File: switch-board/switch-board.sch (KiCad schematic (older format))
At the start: 52 parts, among them IC1 OPTO-TRANSISTOR4, IC2 OPTO-TRANSISTOR4, IC3 OPTO-TRANSISTOR4, IC4 OPTO-TRANSISTOR4, IC5 OPTO-TRANSISTOR4, IC6 OPTO-TRANSISTOR4, IC7 OPTO-TRANSISTOR4, IC8 OPTO-TRANSISTOR4, P1 CONN_01X04, P2 CONN_01X04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

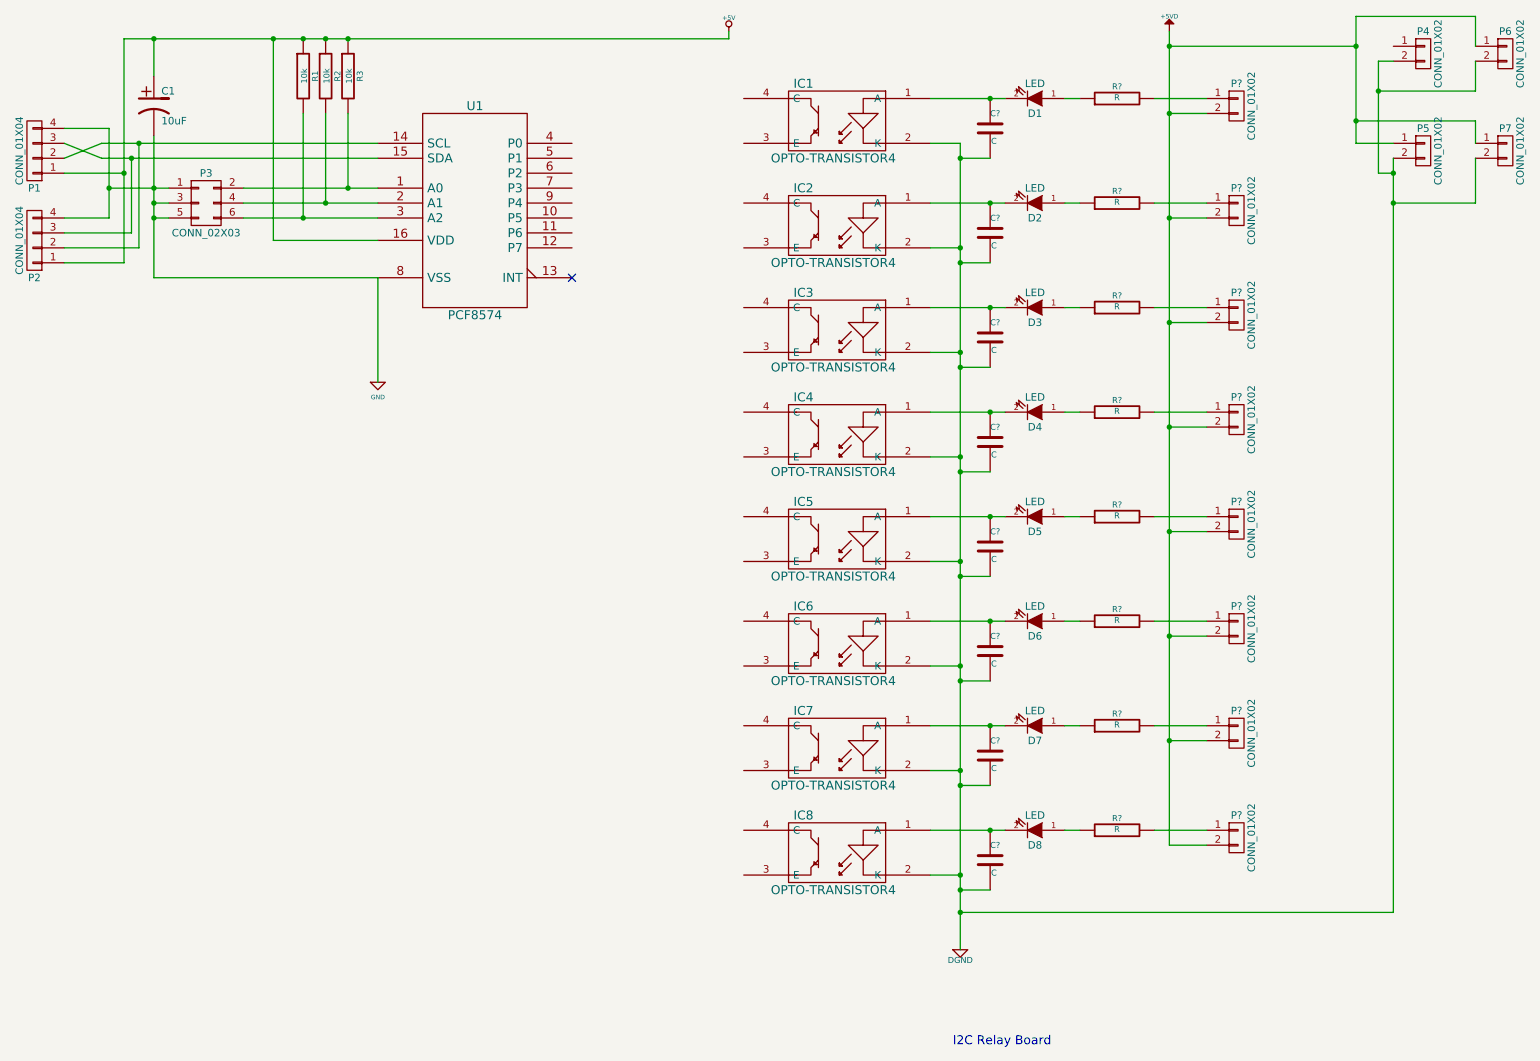
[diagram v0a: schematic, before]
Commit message: completed switches board scheme
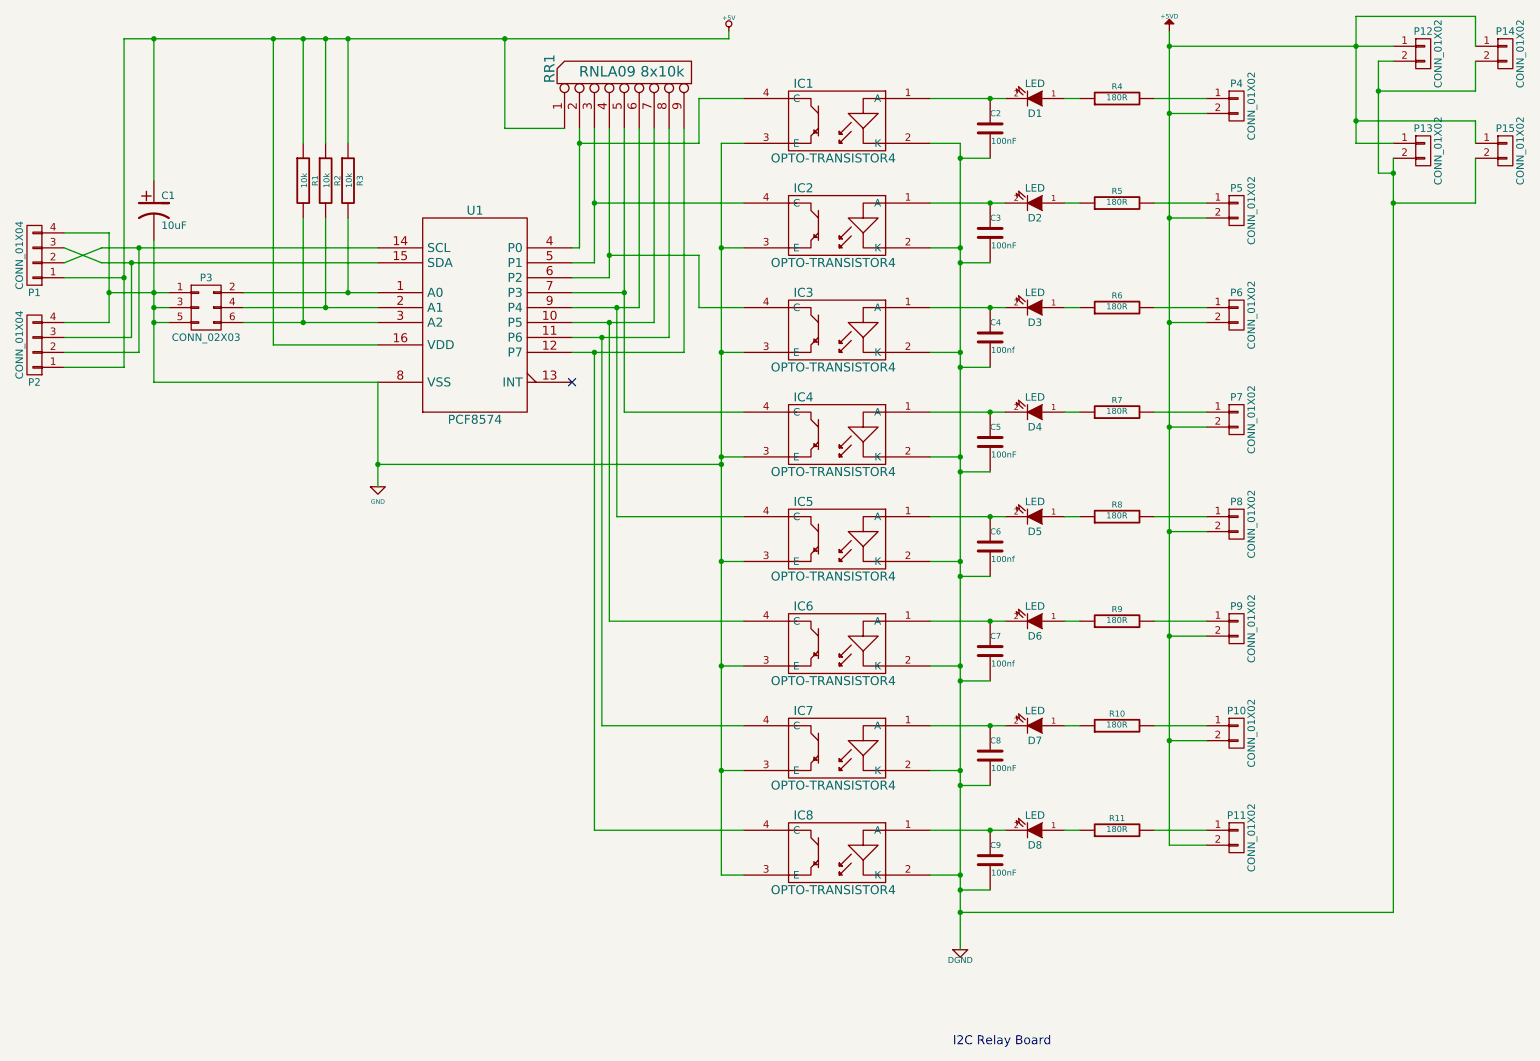
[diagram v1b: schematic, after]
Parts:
- added RR1: RNLA09 8x10k, ~, symbol RR8
- C2, C3, C5, C8, C9: renamed from C?; value C -> 100nF
- C4, C6, C7: renamed from C?; value C -> 100nf
- R10, R11, R4, R5, R6, R7, R8, R9: renamed from R?; value R -> 180R
- gave numbers to parts that had none: 8
- renumbered P4 to P12, P5 to P13, P6 to P14, P7 to P15
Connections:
- net +5V: now also RR1.1 (COM)
- net +5VD: now also P12.1 (P1)
- net GND: now also IC1.3 (E), IC2.3 (E), IC3.3 (E), IC4.3 (E), IC5.3 (E), IC6.3 (E), IC7.3 (E), IC8.3 (E)
- net at U1.10 (P5): now also IC6.4 (C), RR1.7
- net at U1.11 (P6): now also IC7.4 (C), RR1.8
- net at U1.12 (P7): now also IC8.4 (C), RR1.9
- net at U1.4 (P0): now also IC1.4 (C), RR1.2
- net at U1.5 (P1): now also IC2.4 (C), RR1.3
- net at U1.6 (P2): now also IC3.4 (C), RR1.4
- net at U1.7 (P3): now also IC4.4 (C), RR1.5
- net at U1.9 (P4): now also IC5.4 (C), RR1.6
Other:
- moved on the sheet: C1, P1, P2, P3, R1, R2, R3, U1
